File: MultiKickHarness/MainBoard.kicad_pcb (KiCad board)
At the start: 2 copper layers, 76.2 x 49.5 mm, 27 parts, among them J1 Mortal Kombat 1 Y-Unit, J2 Mortal Kombat 1 T-Unit, J3 Mortal Kombat 2, J4 Mortal Kombat 3, J5 Ultimate Mortal Kombat 3, J6 Mortal Kombat 4, J6D1 P1RUN, J6D2 P2RUN, P0 CONN_01X01, P1 TO CONTROL PANEL

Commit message: Revision 2
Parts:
- removed J6D1: P1RUN, Diodes_SMD:MiniMELF_Standard
- removed J6D2: P2RUN, Diodes_SMD:MiniMELF_Standard
- removed the P0 at (85.7, 100.3)
- removed the P0 at (155.6, 100.3)
- removed the P0 at (155.6, 143.5)
- removed the P0 at (85.7, 143.5)
- added J6D3: P1RUN, Diodes_SMD:MiniMELF_Standard, F.Cu at (154.9, 118.1)
- added J6D6: P2RUN, Diodes_SMD:MiniMELF_Standard, F.Cu at (154.9, 133.3)
- added P0: MOUNTING HOLE, Mounting_Holes:MountingHole_3-5mm, F.Cu at (161.3, 100.3)
- added P0: MOUNTING HOLE, Mounting_Holes:MountingHole_3-5mm, F.Cu at (161.3, 143.5)
- added P0: MOUNTING HOLE, Mounting_Holes:MountingHole_3-5mm, F.Cu at (85.1, 143.5)
- added P0: MOUNTING HOLE, Mounting_Holes:MountingHole_3-5mm, F.Cu at (85.1, 100.3)
- added REF**: Symbol_OSHW-Logo_SilkScreen, Symbols:Symbol_OSHW-Logo_SilkScreen, B.Cu at (118.1, 114.3)
- D14: value P2LP -> P2LK
- P1: footprint Pin_Headers:Pin_Header_Angled_1x15 -> Pin_Headers:Pin_Header_Straight_1x15
- moved D1 14.0 mm to (94.0, 128.3)
- moved D8 11.1 mm to (119.4, 123.2)
- moved D6 10.2 mm to (94.0, 121.9)
- moved D11 9.61 mm to (119.4, 129.5)
- moved D10 9.25 mm to (132.1, 135.9)
- moved D5 8.98 mm to (119.4, 142.2)
- moved D2 8.98 mm to (119.4, 135.9)
- moved D9 6.87 mm to (144.8, 123.2)
- moved D7 6.38 mm to (94.0, 115.6)
- moved D13 6.35 mm to (144.8, 129.5)
- moved D12 5.68 mm to (132.1, 142.2)
- moved D3 5.39 mm to (144.8, 135.9)
- moved D4 5.12 mm to (94.0, 134.6)
- moved D14 4.58 mm to (144.8, 142.2)
- moved J6 4.44 mm to (151.1, 108.0)
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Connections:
- net Net-(D1-Pad3) renamed /P2-LP
- net Net-(D10-Pad3) renamed /P1-RUN
- net Net-(D11-Pad3) renamed /P1-LK
- net Net-(D12-Pad3) renamed /P2-RUN
- net Net-(D14-Pad3) renamed /P2-LK
- net Net-(D7-Pad3) renamed /P1-LP
- J1 pad 10: (no net) -> Net-(D6-Pad1)
- J1 pad 11: Net-(D6-Pad1) -> (no net)
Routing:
- net /GND: track 135.3 -> 0.00 mm
- net /P1-LK: track 73.5 -> 95.8 mm
- net Net-(D1-Pad2): track 26.3 -> 7.47 mm
- net Net-(D1-Pad1): track 4.88 -> 22.6 mm
- net /P1-LP: track 75.9 -> 88.6 mm
- net Net-(D6-Pad1): track 4.88 -> 14.6 mm
- net /P2-LK: track 130.7 -> 139.7 mm
- net Net-(D7-Pad2): track 5.51 -> 13.4 mm
- net Net-(D10-Pad2): track 4.88 -> 11.6 mm
- net Net-(D7-Pad1): track 7.36 -> 14.0 mm
- net Net-(D8-Pad2): track 12.1 -> 5.81 mm
- net Net-(D8-Pad1): track 12.1 -> 5.81 mm
- net Net-(D10-Pad1): track 4.88 -> 10.9 mm
- net /P2-RUN: track 75.7 -> 80.8 mm
- net Net-(J6-Pad9): track 5.14 -> 10.1 mm
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- added copper zone on B.Cu, net /GND
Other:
- board size 76.2 x 49.5 mm -> 83.8 x 50.8 mm
- net class Default: clearance 0.2 -> 0.15
- rule trace_clearance: 0.2 -> 0.15
- board text added: "1"
- board text added: "12"
- board text added: "15"
- board text added: "Rev.2"

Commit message: Revision 2 cleaned up
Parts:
- moved REF** 8.89 mm to (118.1, 123.2)
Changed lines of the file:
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@@
   )
   (module Symbols:Symbol_OSHW-Logo_SilkScreen (layer B.Cu)
-    (at 118.11 114.3 270)
+    (at 118.11 123.19 270)
     (descr "Symbol, OSHW-Logo, Silk Screen,")
     (tags "Symbol, OSHW-Logo, Silk Screen,")
@@
     (effects (font (size 1 1) (thickness 0.2)))
   )
-  (gr_text Rev.2 (at 119.38 125.73 90) (layer B.SilkS)
+  (gr_text Rev.2 (at 132.08 123.19 90) (layer B.SilkS)
     (effects (font (size 1.5 1.5) (thickness 0.3)) (justify mirror))
   )
@@
   )
   (dimension 50.8 (width 0.3) (layer Cmts.User)
-    (gr_text "50,800 mm" (at 76.981452 121.704669 270) (layer Cmts.User)
+    (gr_text "50,800 mm" (at 78.66 121.92 270) (layer Cmts.User)
       (effects (font (size 1.5 1.5) (thickness 0.3)))
     )
-    (feature1 (pts (xy 82.141452 147.104669) (xy 75.631452 147.104669)))
-    (feature2 (pts (xy 82.141452 96.304669) (xy 75.631452 96.304669)))
-    (crossbar (pts (xy 78.331452 96.304669) (xy 78.331452 147.104669)))
-    (arrow1a (pts (xy 78.331452 147.104669) (xy 77.745031 145.978165)))
-    (arrow1b (pts (xy 78.331452 147.104669) (xy 78.917873 145.978165)))
-    (arrow2a (pts (xy 78.331452 96.304669) (xy 77.745031 97.431173)))
-    (arrow2b (pts (xy 78.331452 96.304669) (xy 78.917873 97.431173)))
+    (feature1 (pts (xy 83.078501 147.32) (xy 77.31 147.32)))
+    (feature2 (pts (xy 83.078501 96.52) (xy 77.31 96.52)))
+    (crossbar (pts (xy 80.01 96.52) (xy 80.01 147.32)))
+    (arrow1a (pts (xy 80.01 147.32) (xy 79.423579 146.193496)))
+    (arrow1b (pts (xy 80.01 147.32) (xy 80.596421 146.193496)))
+    (arrow2a (pts (xy 80.01 96.52) (xy 79.423579 97.646504)))
+    (arrow2b (pts (xy 80.01 96.52) (xy 80.596421 97.646504)))
   )
   (dimension 83.82 (width 0.3) (layer Cmts.User)
-    (gr_text "83,820 mm" (at 123.19 153.021693) (layer Cmts.User)
+    (gr_text "83,820 mm" (at 123.19 150.514818) (layer Cmts.User)
       (effects (font (size 1.5 1.5) (thickness 0.3)))
     )
-    (feature1 (pts (xy 165.1 146.591694) (xy 165.1 154.371693)))
-    (feature2 (pts (xy 81.28 146.591694) (xy 81.28 154.371693)))
-    (crossbar (pts (xy 81.28 151.671693) (xy 165.1 151.671693)))
-    (arrow1a (pts (xy 165.1 151.671693) (xy 163.973496 152.258114)))
-    (arrow1b (pts (xy 165.1 151.671693) (xy 163.973496 151.085272)))
-    (arrow2a (pts (xy 81.28 151.671693) (xy 82.406504 152.258114)))
-    (arrow2b (pts (xy 81.28 151.671693) (xy 82.406504 151.085272)))
+    (feature1 (pts (xy 165.1 145.686567) (xy 165.1 151.864818)))
+    (feature2 (pts (xy 81.28 145.686567) (xy 81.28 151.864818)))
+    (crossbar (pts (xy 81.28 149.164818) (xy 165.1 149.164818)))
+    (arrow1a (pts (xy 165.1 149.164818) (xy 163.973496 149.751239)))
+    (arrow1b (pts (xy 165.1 149.164818) (xy 163.973496 148.578397)))
+    (arrow2a (pts (xy 81.28 149.164818) (xy 82.406504 149.751239)))
+    (arrow2b (pts (xy 81.28 149.164818) (xy 82.406504 148.578397)))
   )
   (gr_arc (start 85.09 100.33) (end 81.28 100.33) (angle 90) (layer Edge.Cuts) (width 0.5))

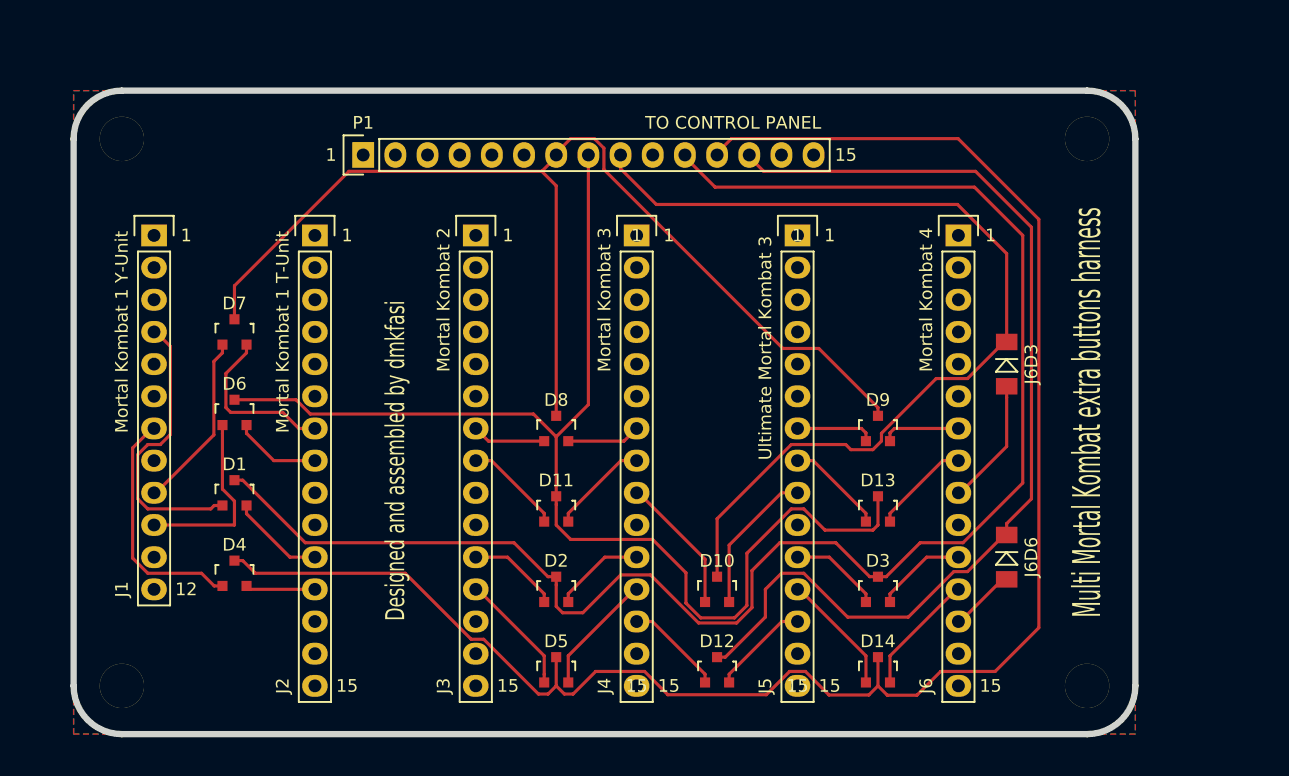
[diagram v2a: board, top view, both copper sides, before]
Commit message: Moved ruler to User.drwg, slightly narrowed board for better sit of P1 control panel connector and moved its name to a place where it is going to be visible after soldering angled pin header
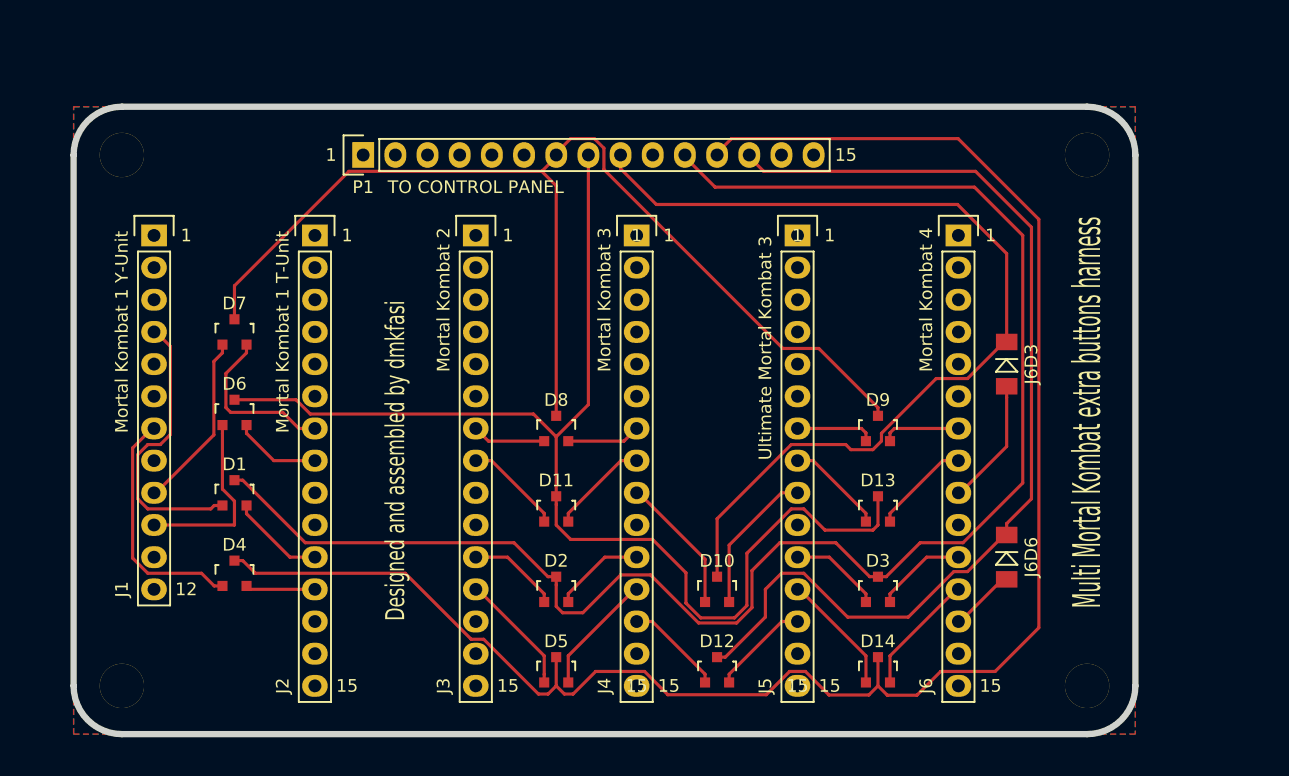
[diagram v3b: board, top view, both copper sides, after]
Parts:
- moved P0 1.27 mm to (161.3, 101.6)
- moved P0 1.27 mm to (85.1, 101.6)
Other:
- board size 83.8 x 50.8 mm -> 83.8 x 49.5 mm

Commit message: New layout
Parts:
- removed J6D3: P1RUN, Diodes_SMD:MiniMELF_Standard
- removed J6D6: P2RUN, Diodes_SMD:MiniMELF_Standard
- added D15: P1RUN, TO_SOT_Packages_SMD:SOT-23, F.Cu at (165.1, 127.0)
- added D16: P2RUN, TO_SOT_Packages_SMD:SOT-23, F.Cu at (165.1, 134.6)
- moved D10 10.9 mm to (138.4, 127.0)
- moved D14 9.92 mm to (152.4, 135.9)
- moved D3 9.16 mm to (152.4, 130.8)
- moved P0 8.98 mm to (170.2, 100.3)
- moved P0 8.89 mm to (170.2, 143.4)
- moved J6 8.89 mm to (160.0, 108.0)
- moved D13 8.52 mm to (152.4, 125.7)
- moved D5 8.13 mm to (124.5, 135.9)
- moved D12 8.13 mm to (138.4, 137.2)
- moved D9 8.03 mm to (152.4, 120.7)
- moved J5 7.62 mm to (146.1, 108.0)
- moved D2 7.18 mm to (124.5, 130.8)
- moved J4 6.35 mm to (132.1, 108.0)
- moved REF** 6.35 mm to (124.5, 123.2)
- moved D11 6.35 mm to (124.5, 125.7)
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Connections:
- J1 pad 11: (no net) -> Net-(J1-Pad11)
- J1 pad 12: (no net) -> Net-(J1-Pad12)
- J1 pad 2: (no net) -> Net-(J1-Pad2)
- J1 pad 3: (no net) -> Net-(J1-Pad3)
- J1 pad 5: (no net) -> Net-(J1-Pad5)
- J1 pad 6: (no net) -> Net-(J1-Pad6)
- J1 pad 8: (no net) -> Net-(J1-Pad8)
- J2 pad 10: (no net) -> Net-(J2-Pad10)
- J2 pad 13: (no net) -> Net-(J2-Pad13)
- J2 pad 14: (no net) -> Net-(J2-Pad14)
- J2 pad 15: (no net) -> Net-(J2-Pad15)
- J2 pad 2: (no net) -> Net-(J2-Pad2)
- J2 pad 3: (no net) -> Net-(J2-Pad3)
- J2 pad 4: (no net) -> Net-(J2-Pad4)
- J2 pad 5: (no net) -> Net-(J2-Pad5)
- J2 pad 6: (no net) -> Net-(J2-Pad6)
- J2 pad 9: (no net) -> Net-(J2-Pad9)
- J3 pad 10: (no net) -> Net-(J3-Pad10)
- J3 pad 13: (no net) -> Net-(J3-Pad13)
- J3 pad 14: (no net) -> Net-(J3-Pad14)
- J3 pad 15: (no net) -> Net-(J3-Pad15)
- J3 pad 2: (no net) -> Net-(J3-Pad2)
- J3 pad 3: (no net) -> Net-(J3-Pad3)
- J3 pad 4: (no net) -> Net-(J3-Pad4)
- J3 pad 5: (no net) -> Net-(J3-Pad5)
- J3 pad 6: (no net) -> Net-(J3-Pad6)
- J3 pad 9: (no net) -> Net-(J3-Pad9)
- J4 pad 10: (no net) -> Net-(J4-Pad10)
- J4 pad 14: (no net) -> Net-(J4-Pad14)
- J4 pad 15: (no net) -> Net-(J4-Pad15)
- J4 pad 2: (no net) -> Net-(J4-Pad2)
- J4 pad 3: (no net) -> Net-(J4-Pad3)
- J4 pad 4: (no net) -> Net-(J4-Pad4)
- J4 pad 5: (no net) -> Net-(J4-Pad5)
- J4 pad 6: (no net) -> Net-(J4-Pad6)
- J5 pad 10: (no net) -> Net-(J5-Pad10)
- J5 pad 14: (no net) -> Net-(J5-Pad14)
- J5 pad 15: (no net) -> Net-(J5-Pad15)
- J5 pad 2: (no net) -> Net-(J5-Pad2)
- J5 pad 3: (no net) -> Net-(J5-Pad3)
- J5 pad 4: (no net) -> Net-(J5-Pad4)
- J5 pad 5: (no net) -> Net-(J5-Pad5)
- J5 pad 6: (no net) -> Net-(J5-Pad6)
- J6 pad 10: (no net) -> Net-(J6-Pad10)
- J6 pad 14: (no net) -> Net-(J6-Pad14)
- J6 pad 15: (no net) -> Net-(J6-Pad15)
- J6 pad 2: (no net) -> Net-(J6-Pad2)
- J6 pad 3: (no net) -> Net-(J6-Pad3)
- J6 pad 4: (no net) -> Net-(J6-Pad4)
- J6 pad 5: (no net) -> Net-(J6-Pad5)
- J6 pad 6: (no net) -> Net-(J6-Pad6)
- P1 pad 10: (no net) -> Net-(P1-Pad10)
- P1 pad 14: (no net) -> Net-(P1-Pad14)
- P1 pad 15: (no net) -> Net-(P1-Pad15)
- P1 pad 2: (no net) -> Net-(P1-Pad2)
- P1 pad 3: (no net) -> Net-(P1-Pad3)
- P1 pad 4: (no net) -> Net-(P1-Pad4)
- P1 pad 5: (no net) -> Net-(P1-Pad5)
- P1 pad 6: (no net) -> Net-(P1-Pad6)
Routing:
- net /P2-LK: track 139.7 -> 0.00 mm
- net /P2-LP: track 128.2 -> 0.00 mm
- net /P1-LK: track 95.8 -> 0.00 mm
- net /P1-LP: track 88.6 -> 0.00 mm
- net /P2-RUN: track 80.8 -> 0.00 mm
- net /P1-RUN: track 75.2 -> 0.00 mm
- net Net-(D1-Pad1): track 22.6 -> 0.00 mm
- net Net-(D4-Pad1): track 19.0 -> 0.00 mm
- net Net-(D6-Pad1): track 14.6 -> 0.00 mm
- net Net-(D7-Pad1): track 14.0 -> 0.00 mm
- net Net-(D7-Pad2): track 13.4 -> 0.00 mm
- net Net-(D10-Pad2): track 11.6 -> 0.00 mm
- net Net-(D10-Pad1): track 10.9 -> 0.00 mm
- net Net-(D15-Pad1): track 10.1 -> 0.00 mm
- net Net-(D5-Pad2): track 9.68 -> 0.00 mm
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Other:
- board size 83.8 x 49.5 mm -> 95.3 x 50.8 mm
- net class Default: clearance 0.15 -> 0.2
- rule trace_clearance: 0.15 -> 0.2
- board text added: "Rev.2.1"
- board text removed: "12"
- board text removed: "Rev.2"

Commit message: Complete Rev.2.1
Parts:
- moved D16 2.54 mm to (165.1, 137.2)
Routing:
- net /P2-LK: track 0.00 -> 95.7 mm, vias 0 -> 1
- net /P2-LP: track 0.00 -> 89.2 mm, vias 0 -> 1
- net /P1-LK: track 0.00 -> 81.0 mm, vias 0 -> 2
- net /P1-RUN: track 0.00 -> 78.1 mm, vias 0 -> 1
- net /P1-LP: track 0.00 -> 76.6 mm
- net /P2-RUN: track 0.00 -> 72.8 mm, vias 0 -> 2
- net Net-(D4-Pad1): track 0.00 -> 21.0 mm
- net Net-(D1-Pad1): track 0.00 -> 20.1 mm
- net Net-(D7-Pad1): track 0.00 -> 8.82 mm
- net Net-(D7-Pad2): track 0.00 -> 7.69 mm
- net Net-(D6-Pad1): track 0.00 -> 7.42 mm
- net Net-(D3-Pad2): track 0.00 -> 7.40 mm
- net Net-(D2-Pad2): track 0.00 -> 7.40 mm
- net Net-(D9-Pad2): track 0.00 -> 7.40 mm
- net Net-(D8-Pad2): track 0.00 -> 7.31 mm
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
